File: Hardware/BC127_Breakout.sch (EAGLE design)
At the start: 38 parts, among them Q1 MOSFET-NCHANNELBSS138, Q2 MOSFET-NCHANNELBSS138, Q3 MMBT4403, U2 MIC5219 3.3V

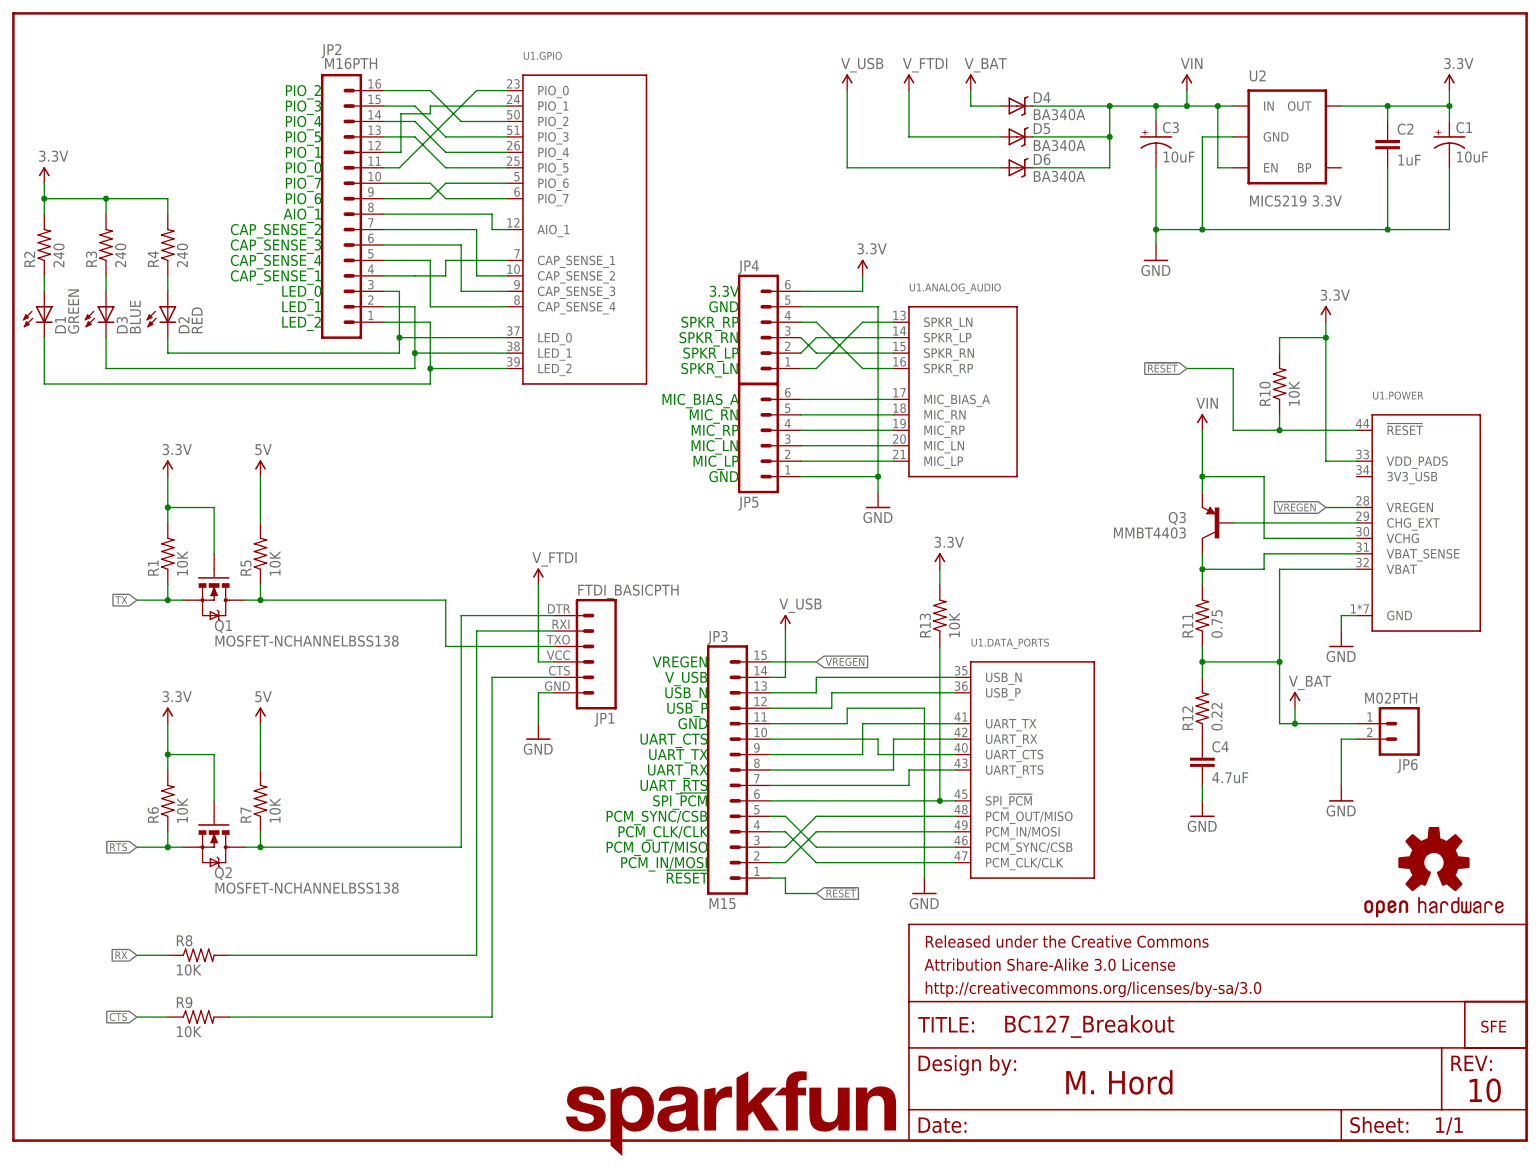
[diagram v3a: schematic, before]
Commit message: Changed TCream
-Changed TCream for more paste application to allow for better reflow to
the BC127 module
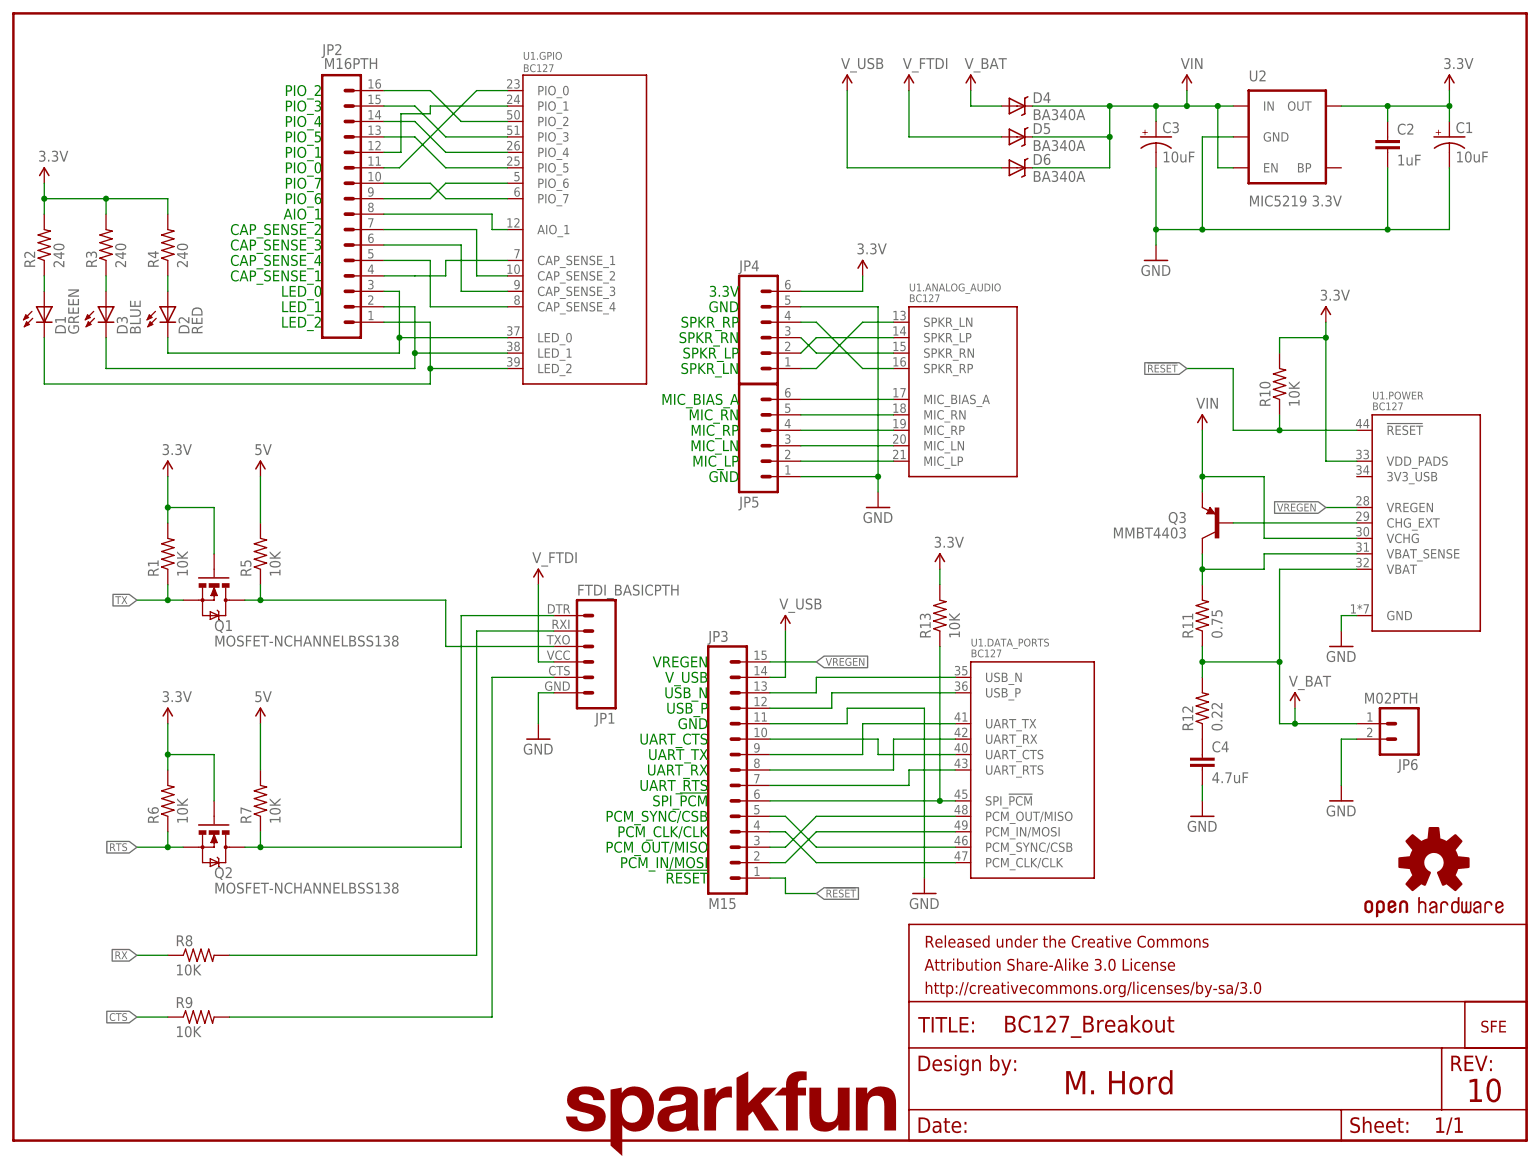
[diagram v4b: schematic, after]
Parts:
- U1: value (none) -> BC127; device SparkFun-RF:BC127 -> SparkFun-RF:BC127EXTRA_PASTE
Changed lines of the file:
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@@
 <grid distance="0.1" unitdist="inch" unit="inch" style="lines" multiple="1" display="no" altdistance="0.01" altunitdist="inch" altunit="inch"/>
 <layers>
-<layer number="1" name="Top" color="4" fill="1" visible="no" active="no"/>
-<layer number="2" name="Route2" color="1" fill="3" visible="no" active="no"/>
-<layer number="3" name="Route3" color="4" fill="3" visible="no" active="no"/>
-<layer number="4" name="Route4" color="1" fill="4" visible="no" active="no"/>
-<layer number="5" name="Route5" color="4" fill="4" visible="no" active="no"/>
-<layer number="6" name="Route6" color="1" fill="8" visible="no" active="no"/>
-<layer number="7" name="Route7" color="4" fill="8" visible="no" active="no"/>
-<layer number="8" name="Route8" color="1" fill="2" visible="no" active="no"/>
-<layer number="9" name="Route9" color="4" fill="2" visible="no" active="no"/>
-<layer number="10" name="Route10" color="1" fill="7" visible="no" active="no"/>
-<layer number="11" name="Route11" color="4" fill="7" visible="no" active="no"/>
-<layer number="12" name="Route12" color="1" fill="5" visible="no" active="no"/>
-<layer number="13" name="Route13" color="4" fill="5" visible="no" active="no"/>
-<layer number="14" name="Route14" color="1" fill="6" visible="no" active="no"/>
-<layer number="15" name="Route15" color="4" fill="6" visible="no" active="no"/>
-<layer number="16" name="Bottom" color="1" fill="1" visible="no" active="no"/>
-<layer number="17" name="Pads" color="2" fill="1" visible="no" active="no"/>
-<layer number="18" name="Vias" color="2" fill="1" visible="no" active="no"/>
-<layer number="19" name="Unrouted" color="6" fill="1" visible="no" active="no"/>
-<layer number="20" name="Dimension" color="15" fill="1" visible="no" active="no"/>
-<layer number="21" name="tPlace" color="16" fill="1" visible="no" active="no"/>
-<layer number="22" name="bPlace" color="14" fill="1" visible="no" active="no"/>
-<layer number="23" name="tOrigins" color="15" fill="1" visible="no" active="no"/>
-<layer number="24" name="bOrigins" color="15" fill="1" visible="no" active="no"/>
-<layer number="25" name="tNames" color="7" fill="1" visible="no" active="no"/>
-<layer number="26" name="bNames" color="7" fill="1" visible="no" active="no"/>
-<layer number="27" name="tValues" color="7" fill="1" visible="no" active="no"/>
-<layer number="28" name="bValues" color="7" fill="1" visible="no" active="no"/>
+<layer number="1" name="Top" color="4" fill="1" visible="yes" active="no"/>
+<layer number="2" name="Route2" color="1" fill="3" visible="yes" active="no"/>
+<layer number="3" name="Route3" color="4" fill="3" visible="yes" active="no"/>
+<layer number="4" name="Route4" color="1" fill="4" visible="yes" active="no"/>
+<layer number="5" name="Route5" color="4" fill="4" visible="yes" active="no"/>
+<layer number="6" name="Route6" color="1" fill="8" visible="yes" active="no"/>
+<layer number="7" name="Route7" color="4" fill="8" visible="yes" active="no"/>
+<layer number="8" name="Route8" color="1" fill="2" visible="yes" active="no"/>
+<layer number="9" name="Route9" color="4" fill="2" visible="yes" active="no"/>
+<layer number="10" name="Route10" color="1" fill="7" visible="yes" active="no"/>
+<layer number="11" name="Route11" color="4" fill="7" visible="yes" active="no"/>
+<layer number="12" name="Route12" color="1" fill="5" visible="yes" active="no"/>
+<layer number="13" name="Route13" color="4" fill="5" visible="yes" active="no"/>
+<layer number="14" name="Route14" color="1" fill="6" visible="yes" active="no"/>
+<layer number="15" name="Route15" color="4" fill="6" visible="yes" active="no"/>
+<layer number="16" name="Bottom" color="1" fill="1" visible="yes" active="no"/>
+<layer number="17" name="Pads" color="2" fill="1" visible="yes" active="no"/>
+<layer number="18" name="Vias" color="2" fill="1" visible="yes" active="no"/>
+<layer number="19" name="Unrouted" color="6" fill="1" visible="yes" active="no"/>
+<layer number="20" name="Dimension" color="6" fill="1" visible="yes" active="no"/>
+<layer number="21" name="tPlace" color="16" fill="1" visible="yes" active="no"/>
+<layer number="22" name="bPlace" color="14" fill="1" visible="yes" active="no"/>
+<layer number="23" name="tOrigins" color="15" fill="1" visible="yes" active="no"/>
+<layer number="24" name="bOrigins" color="15" fill="1" visible="yes" active="no"/>
+<layer number="25" name="tNames" color="7" fill="1" visible="yes" active="no"/>
+<layer number="26" name="bNames" color="7" fill="1" visible="yes" active="no"/>
+<layer number="27" name="tValues" color="7" fill="1" visible="yes" active="no"/>
+<layer number="28" name="bValues" color="7" fill="1" visible="yes" active="no"/>
 <layer number="29" name="tStop" color="7" fill="3" visible="no" active="no"/>
 <layer number="30" name="bStop" color="7" fill="6" visible="no" active="no"/>
@@
 <layer number="35" name="tGlue" color="7" fill="4" visible="no" active="no"/>
 <layer number="36" name="bGlue" color="7" fill="5" visible="no" active="no"/>
-<layer number="37" name="tTest" color="7" fill="1" visible="no" active="no"/>
-<layer number="38" name="bTest" color="7" fill="1" visible="no" active="no"/>
+<layer number="37" name="tTest" color="7" fill="1" visible="yes" active="no"/>
+<layer number="38" name="bTest" color="7" fill="1" visible="yes" active="no"/>
 <layer number="39" name="tKeepout" color="4" fill="11" visible="no" active="no"/>
 <layer number="40" name="bKeepout" color="1" fill="11" visible="no" active="no"/>
@@
 <layer number="44" name="Drills" color="7" fill="1" visible="no" active="no"/>
 <layer number="45" name="Holes" color="7" fill="1" visible="no" active="no"/>
-<layer number="46" name="Milling" color="3" fill="1" visible="no" active="no"/>
-<layer number="47" name="Measures" color="7" fill="1" visible="no" active="no"/>
-<layer number="48" name="Document" color="7" fill="1" visible="no" active="no"/>
-<layer number="49" name="Reference" color="7" fill="1" visible="no" active="no"/>
-<layer number="50" name="dxf" color="7" fill="1" visible="no" active="no"/>
-<layer number="51" name="tDocu" color="6" fill="1" visible="no" active="no"/>
-<layer number="52" name="bDocu" color="7" fill="1" visible="no" active="no"/>
-<layer number="53" name="tGND_GNDA" color="7" fill="9" visible="no" active="no"/>
-<layer number="54" name="bGND_GNDA" color="1" fill="9" visible="no" active="no"/>
-<layer number="56" name="wert" color="7" fill="1" visible="no" active="no"/>
+<layer number="46" name="Milling" color="3" fill="1" visible="yes" active="no"/>
+<layer number="47" name="Measures" color="7" fill="1" visible="yes" active="no"/>
+<layer number="48" name="Document" color="7" fill="1" visible="yes" active="no"/>
+<layer number="49" name="Reference" color="7" fill="1" visible="yes" active="no"/>
+<layer number="50" name="dxf" color="7" fill="1" visible="yes" active="no"/>
+<layer number="51" name="tDocu" color="6" fill="1" visible="yes" active="no"/>
+<layer number="52" name="bDocu" color="7" fill="1" visible="yes" active="no"/>
+<layer number="53" name="tGND_GNDA" color="7" fill="9" visible="yes" active="no"/>
+<layer number="54" name="bGND_GNDA" color="1" fill="9" visible="yes" active="no"/>
+<layer number="56" name="wert" color="7" fill="1" visible="yes" active="no"/>
 <layer number="91" name="Nets" color="2" fill="1" visible="yes" active="yes"/>
 <layer number="92" name="Busses" color="1" fill="1" visible="yes" active="yes"/>
@@
 </classes>
 <parts>
-<part name="U1" library="SparkFun-RF" deviceset="BC127" device=""/>
+<part name="U1" library="SparkFun-RF" deviceset="BC127" device="EXTRA_PASTE" value="BC127"/>
 <part name="Q1" library="SparkFun-DiscreteSemi" deviceset="MOSFET-NCHANNEL" device="BSS138"/>
 <part name="U2" library="SparkFun-PowerIC" deviceset="V_REG_MIC5219" device="3.3V" value="MIC5219 3.3V"/>
